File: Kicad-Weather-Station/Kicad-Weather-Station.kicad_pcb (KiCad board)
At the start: 2 copper layers, 100 x 50 mm, 64 parts, among them CON1 Solar Panel, J1 MicroSD, P1 CONN_01X25, P12 CONN_01X01, P2 CONN_01X25, P3 Rain Gauge, P4 Temperature/Humidity, P5 Wind Speed, P6 Air Pressure, P7 Battery, Q1 MMBT3904, Q2 MMBT3904, Q3 MMBT3906, Q4 SUD45P03-12-GE3, Q5 MMBT3904, Q6 MMBT3904, Q7 MMBT3904, Q8 MMBT3906, Q9 SUD45P03-12-GE3, U1 LMV324, U2 78M05, U3 TPS77033

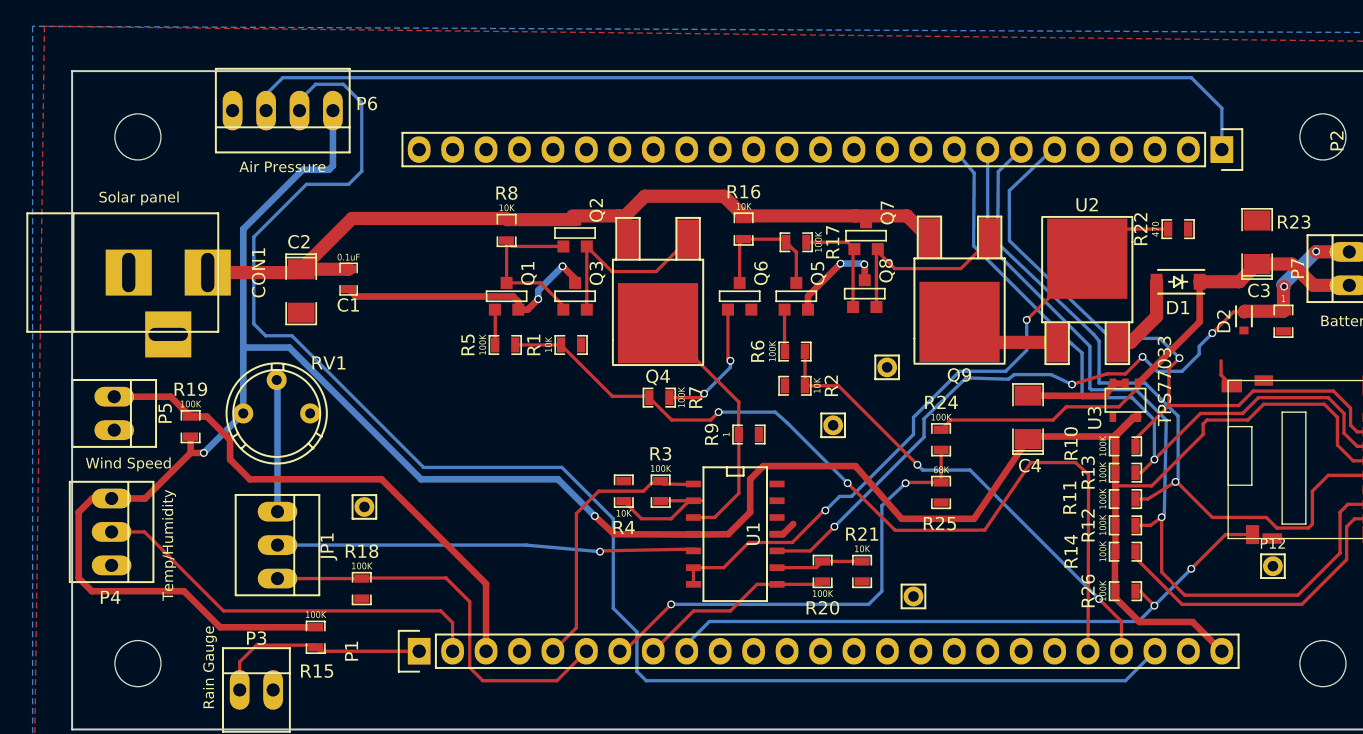
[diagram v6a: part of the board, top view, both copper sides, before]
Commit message: Update schematic and PCB to allow some sensors to be powered off.
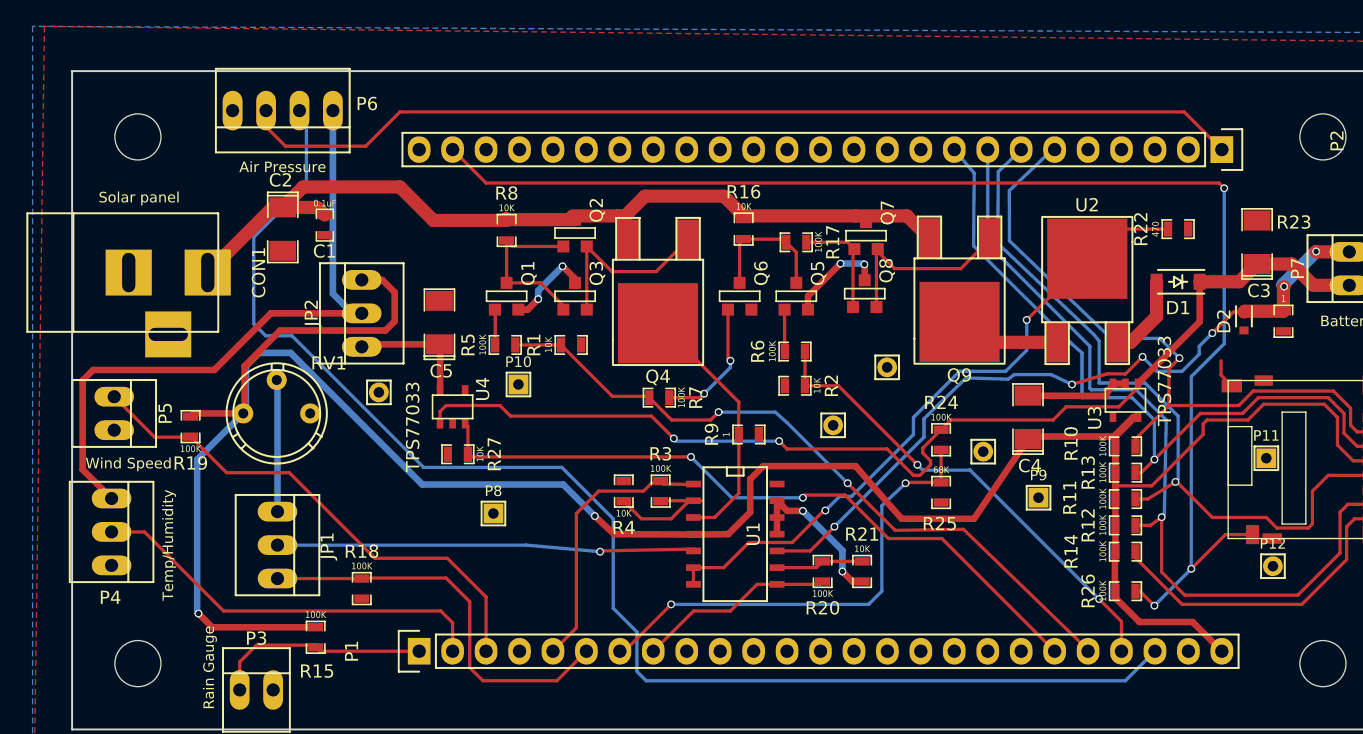
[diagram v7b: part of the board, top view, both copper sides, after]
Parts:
- added C5: 10uF, WeatherStation:SM1206POL, F.Cu at (87.9, 74.1)
- added JP2: JUMPER3, WeatherStation:PINHEAD1-3, F.Cu at (82.0, 73.4)
- added P10: CONN_01X01, WeatherStation:SIL-1, F.Cu at (93.9, 78.8)
- added P11: CONN_01X01, WeatherStation:SIL-1, F.Cu at (150.7, 84.4)
- added P8: CONN_01X01, WeatherStation:SIL-1, F.Cu at (92.0, 88.6)
- added P9: CONN_01X01, WeatherStation:SIL-1, F.Cu at (133.4, 87.4)
- added R27: 10K, WeatherStation:SM0603_Resistor, F.Cu at (89.3, 84.1)
- added U4: TPS77033, WeatherStation:SOT23-5, F.Cu at (88.9, 80.5)
- moved ? 12.2 mm to (129.2, 83.9)
- moved ? 8.77 mm to (83.3, 79.4)
- moved C2 4.90 mm to (76.0, 67.0)
- moved C1 4.48 mm to (79.2, 66.7)
- turned R19 to 90 degrees
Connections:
- net Net-(C3-Pad1) renamed Power
- C4 pad 1: +3.3V -> +3.3V-M
- J1 pad 11: PA8 -> PD2
- J1 pad 4: +3.3V -> +3.3V-M
- P1 pad 20: Net-(P1-Pad20) -> PB3
- P1 pad 25: +3.3V -> +3.3V-M
- P1 pad 9: PA8 -> Net-(P1-Pad9)
- P2 pad 24: Net-(P2-Pad24) -> PD2
- R10 pad 1: +3.3V -> +3.3V-M
- R11 pad 1: +3.3V -> +3.3V-M
- R12 pad 1: +3.3V -> +3.3V-M
- R13 pad 1: +3.3V -> +3.3V-M
- R14 pad 1: +3.3V -> +3.3V-M
- R15 pad 1: +3.3V -> +3.3V-M
- R19 pad 2: +3.3V -> +3.3V-M
- R26 pad 1: +3.3V -> +3.3V-M
- R26 pad 2: PA8 -> PD2
- RV1 pad 1: +3.3V -> +3.3V-M
- U1 pad 12: (no net) -> Earth
- U1 pad 13: (no net) -> Earth
- U1 pad 14: (no net) -> Net-(U1-Pad14)
- U1 pad 4: +3.3V -> +3.3V-M
- U3 pad 5: +3.3V -> +3.3V-M
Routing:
- net +3.3V-M: track 0.00 -> 190.7 mm, vias 0 -> 2
- net +3.3V: track 203.7 -> 49.9 mm, vias 2 -> 0
- net PD2: track 0.00 -> 101.3 mm, vias 0 -> 3
- net PB3: track 0.00 -> 53.3 mm, vias 0 -> 2
- net PA8: track 48.8 -> 0.00 mm, vias 2 -> 0
- net Power: track 38.9 -> 83.2 mm, vias 0 -> 2
- net PB4: track 66.3 -> 53.6 mm
- net PB6: track 115.0 -> 105.2 mm
- net Net-(C5-Pad1): track 0.00 -> 9.48 mm
- net Earth: track 40.3 -> 37.0 mm, vias 4 -> 6
- net PA2: track 40.1 -> 38.7 mm
- net Net-(C1-Pad1): track 68.7 -> 67.3 mm
- net Net-(P1-Pad9): track 0.00 -> 0.54 mm
- net PB7: track 78.4 -> 77.9 mm

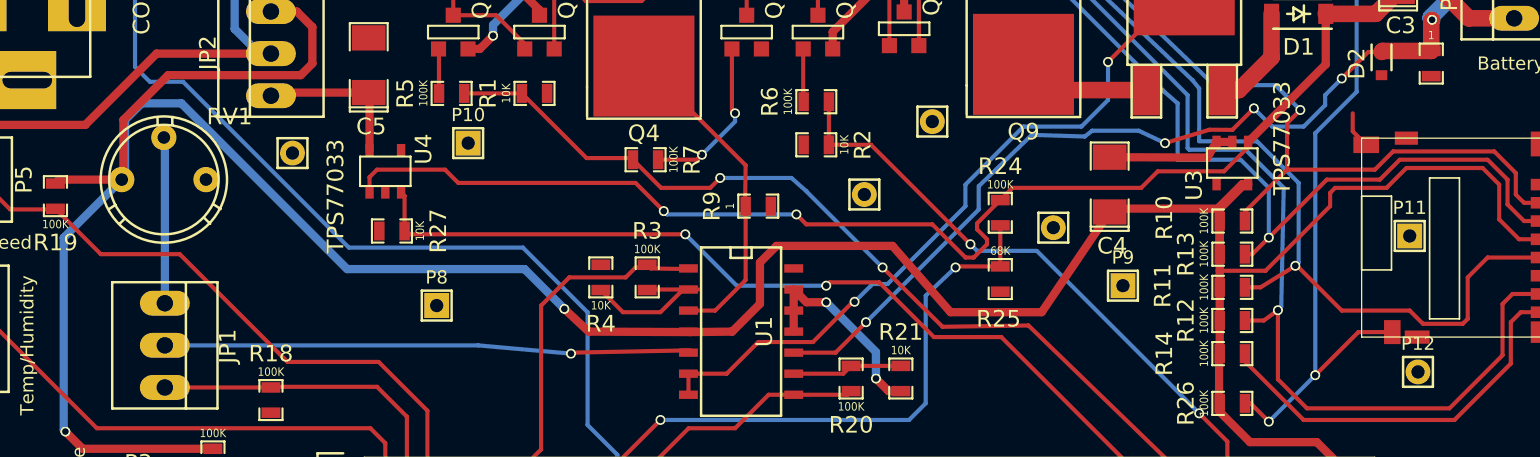
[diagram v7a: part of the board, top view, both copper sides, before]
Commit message: Clean up PCB footprints and generate gerbers.
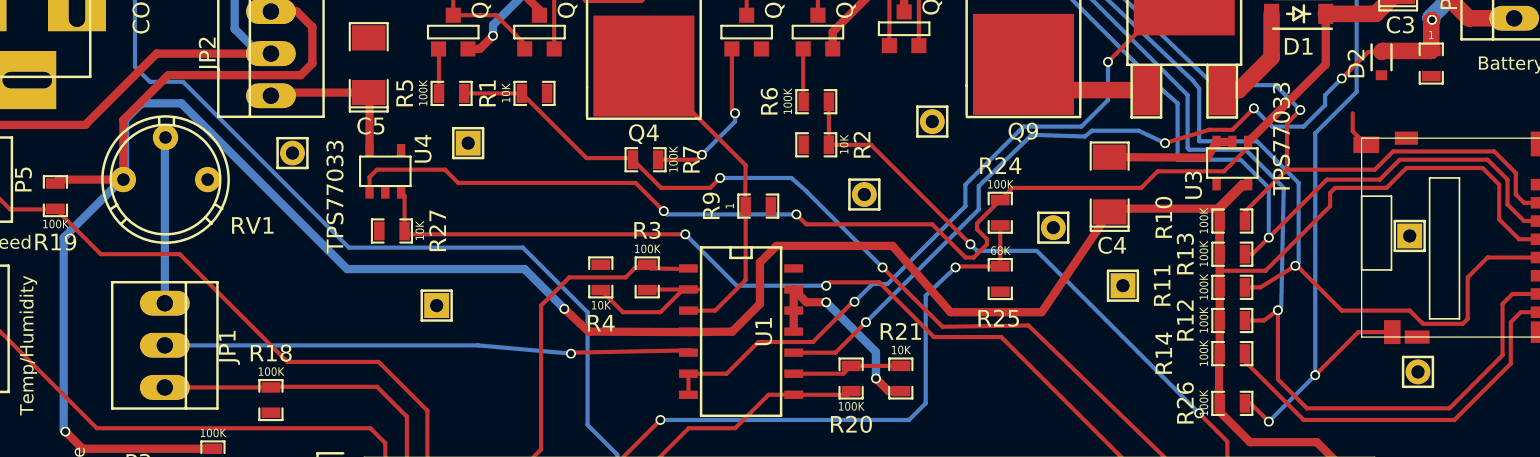
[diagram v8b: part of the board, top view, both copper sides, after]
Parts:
- RV1: footprint Potentiometers:Potentiometer_Bourns_3339P_Angular_ScrewUp -> WeatherStation:Potentiometer_Bourns_3339P_Angular_ScrewUp
- moved RV1 0.10 mm to (73.1, 81.0)
- renumbered P8 to ?, P9 to ?, P10 to ?, P11 to ?, P12 to ?
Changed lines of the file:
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@@
   (layers
     (0 F.Cu signal)
-    (31 B.Cu signal)
+    (31 B.Cu signal hide)
     (32 B.Adhes user hide)
     (33 F.Adhes user hide)
     (34 B.Paste user hide)
     (35 F.Paste user hide)
-    (36 B.SilkS user hide)
+    (36 B.SilkS user)
     (37 F.SilkS user)
-    (38 B.Mask user hide)
-    (39 F.Mask user hide)
-    (40 Dwgs.User user)
+    (38 B.Mask user)
+    (39 F.Mask user)
+    (40 Dwgs.User user hide)
     (41 Cmts.User user)
     (42 Eco1.User user hide)
@@
   )
   (setup
-    (last_trace_width 0.5)
+    (last_trace_width 0.25)
     (user_trace_width 0.5)
     (user_trace_width 1)
@@
     (visible_elements FFFFFF7F)
     (pcbplotparams
-      (layerselection 0x010f0_80000001)
-      (usegerberextensions false)
+      (layerselection 0x010fc_80000001)
+      (usegerberextensions true)
       (excludeedgelayer true)
       (linewidth 0.100000)
@@
       (effects (font (size 1 1) (thickness 0.15)))
     )
-    (fp_text value "Solar Panel" (at 0 -5.99948) (layer F.Fab)
+    (fp_text value "Solar Panel" (at 3.5 -4.3) (layer F.Fab)
       (effects (font (size 1 1) (thickness 0.15)))
     )
@@
       (effects (font (size 1 1) (thickness 0.15)))
     )
-    (fp_text value 1N4148 (at 0 1.7 90) (layer F.Fab)
+    (fp_text value 1N4148 (at -2.5 1.2 180) (layer F.Fab)
       (effects (font (size 1 1) (thickness 0.15)))
     )
@@
       (effects (font (size 1 1) (thickness 0.15)))
     )
-    (fp_text value CONN_01X25 (at 0 -3.1 90) (layer F.Fab)
+    (fp_text value CONN_01X25 (at -3.34 22.74 180) (layer F.Fab)
       (effects (font (size 1 1) (thickness 0.15)))
     )
@@
       (effects (font (size 1 1) (thickness 0.15)))
     )
-    (fp_text value CONN_01X25 (at 0 -3.1 270) (layer F.Fab)
+    (fp_text value CONN_01X25 (at -2.86 35.82 360) (layer F.Fab)
       (effects (font (size 1 1) (thickness 0.15)))
     )
@@
       (effects (font (size 1 1) (thickness 0.15)))
     )
-    (fp_text value "Rain Gauge" (at 0 3.81) (layer F.Fab)
+    (fp_text value "Rain Gauge" (at 0 5.5) (layer F.Fab)
       (effects (font (size 1 1) (thickness 0.15)))
     )
@@
       (effects (font (size 1 1) (thickness 0.15)))
     )
-    (fp_text value "Wind Speed" (at 0 3.81 270) (layer F.Fab)
+    (fp_text value "Wind Speed" (at 0 5.6 270) (layer F.Fab)
       (effects (font (size 1 1) (thickness 0.15)))
     )
@@
       (effects (font (size 1 1) (thickness 0.15)))
     )
-    (fp_text value "Air Pressure" (at 0 3.81 180) (layer F.Fab)
+    (fp_text value "Air Pressure" (at -0.2 5.4 180) (layer F.Fab)
       (effects (font (size 1 1) (thickness 0.15)))
     )
@@
     )
   )
-  (module Potentiometers:Potentiometer_Bourns_3339P_Angular_ScrewUp (layer F.Cu)
-    (at 73 81)
-    (descr "5/16, Round, Trimming, Potentiometer, Bourns, 3339")
-    (tags "5/16, Round, Trimming, Potentiometer, Bourns, 3339")
-    (fp_text reference RV1 (at 6.5 -3.8) (layer F.SilkS)
-      (effects (font (size 1 1) (thickness 0.15)))
-    )
-    (fp_text value 100K (at 2.54 6.35) (layer F.Fab)
-      (effects (font (size 1 1) (thickness 0.15)))
-    )
-    (fp_line (start 5.334 2.667) (end 4.953 2.286) (layer F.SilkS) (width 0.15))
-    (fp_line (start 5.969 1.778) (end 5.588 1.524) (layer F.SilkS) (width 0.15))
-    (fp_line (start -0.762 1.778) (end -0.381 1.524) (layer F.SilkS) (width 0.15))
-    (fp_line (start -0.127 2.667) (end 0.127 2.413) (layer F.SilkS) (width 0.15))
-    (fp_line (start 3.048 -3.302) (end 3.048 -3.683) (layer F.SilkS) (width 0.15))
-    (fp_line (start 2.159 -3.302) (end 2.159 -3.683) (layer F.SilkS) (width 0.15))
-    (fp_circle (center 2.54 0) (end 5.842 0) (layer F.SilkS) (width 0.15))
-    (fp_circle (center 2.54 0) (end 6.35 0) (layer F.SilkS) (width 0.15))
-    (pad 2 thru_hole circle (at 2.54 -2.54) (size 1.524 1.524) (drill 0.762) (layers *.Cu *.Mask F.SilkS)
-      (net 6 "Net-(JP1-Pad1)"))
-    (pad 1 thru_hole circle (at 0 0) (size 1.524 1.524) (drill 0.762) (layers *.Cu *.Mask F.SilkS)
-      (net 70 +3.3V-M))
-    (pad 3 thru_hole circle (at 5.08 0) (size 1.524 1.524) (drill 0.762) (layers *.Cu *.Mask F.SilkS)
-      (net 2 Earth))
-    (model Potentiometers.3dshapes/Potentiometer_Bourns_3339P_Angular_ScrewUp.wrl
-      (at (xyz 0 0 0))
-      (scale (xyz 1 1 1))
-      (rotate (xyz 0 0 0))
-    )
-  )
   (module WeatherStation:MountingHole_3-5mm (layer F.Cu)
     (at 65 100)
@@
       (effects (font (size 1 1) (thickness 0.15)))
     )
-    (fp_text value MountingHole_3-5mm (at 0 5.00126) (layer F.Fab)
+    (fp_text value MountingHole_3-5mm (at -0.1 5.9) (layer F.Fab)
       (effects (font (size 1 1) (thickness 0.15)))
     )
@@
       (effects (font (size 1 1) (thickness 0.15)))
     )
-    (fp_text value MountingHole_3-5mm (at 0 5.00126) (layer F.Fab)
+    (fp_text value MountingHole_3-5mm (at 0.2 5.8) (layer F.Fab)
       (effects (font (size 1 1) (thickness 0.15)))
     )
@@
       (effects (font (size 1 1) (thickness 0.15)))
     )
-    (fp_text value MountingHole_3-5mm (at 0 5.00126) (layer F.Fab)
+    (fp_text value MountingHole_3-5mm (at -0.8 -6.1) (layer F.Fab)
       (effects (font (size 1 1) (thickness 0.15)))
     )
@@
       (effects (font (size 1 1) (thickness 0.15)))
     )
-    (fp_text value MountingHole_3-5mm (at 0 5.00126) (layer F.Fab)
+    (fp_text value MountingHole_3-5mm (at 0.1 -6.1) (layer F.Fab)
       (effects (font (size 1 1) (thickness 0.15)))
     )
@@
     (tags "CONN DEV")
     (zone_connect 2)
-    (fp_text reference P12 (at 0 -1.7) (layer F.SilkS)
+    (fp_text reference "" (at 0 -1.7) (layer F.SilkS)
       (effects (font (size 0.8 0.8) (thickness 0.15)))
     )
@@
     (tags "CONN DEV")
     (zone_connect 2)
-    (fp_text reference P8 (at 0 -1.7) (layer F.SilkS)
+    (fp_text reference "" (at 0 -1.7) (layer F.SilkS)
       (effects (font (size 0.8 0.8) (thickness 0.15)))
     )
@@
     (tags "CONN DEV")
     (zone_connect 2)
-    (fp_text reference P9 (at 0 -1.7) (layer F.SilkS)
+    (fp_text reference "" (at 0 -1.7) (layer F.SilkS)
       (effects (font (size 0.8 0.8) (thickness 0.15)))
     )
@@
     (tags "CONN DEV")
     (zone_connect 2)
-    (fp_text reference P10 (at 0 -1.7) (layer F.SilkS)
+    (fp_text reference "" (at 1.3 2.5) (layer F.SilkS)
       (effects (font (size 0.8 0.8) (thickness 0.15)))
     )
@@
     (tags "CONN DEV")
     (zone_connect 2)
-    (fp_text reference P11 (at 0 -1.7) (layer F.SilkS)
+    (fp_text reference "" (at 0 -1.7) (layer F.SilkS)
       (effects (font (size 0.8 0.8) (thickness 0.15)))
     )
@@
       (rotate (xyz 0 0 0))
     )
+  )
+  (module WeatherStation:Potentiometer_Bourns_3339P_Angular_ScrewUp (layer F.Cu)
+    (at 73.1 81)
+    (descr "5/16, Round, Trimming, Potentiometer, Bourns, 3339")
+    (tags "5/16, Round, Trimming, Potentiometer, Bourns, 3339")
+    (fp_text reference RV1 (at 7.8 2.8) (layer F.SilkS)
+      (effects (font (size 1 1) (thickness 0.15)))
+    )
+    (fp_text value 100K (at 2.54 6.35) (layer F.Fab)
+      (effects (font (size 1 1) (thickness 0.15)))
+    )
+    (fp_line (start 5.334 2.667) (end 4.953 2.286) (layer F.SilkS) (width 0.15))
+    (fp_line (start 5.969 1.778) (end 5.588 1.524) (layer F.SilkS) (width 0.15))
+    (fp_line (start -0.762 1.778) (end -0.381 1.524) (layer F.SilkS) (width 0.15))
+    (fp_line (start -0.127 2.667) (end 0.127 2.413) (layer F.SilkS) (width 0.15))
+    (fp_line (start 3.048 -3.302) (end 3.048 -3.683) (layer F.SilkS) (width 0.15))
+    (fp_line (start 2.159 -3.302) (end 2.159 -3.683) (layer F.SilkS) (width 0.15))
+    (fp_circle (center 2.54 0) (end 5.842 0) (layer F.SilkS) (width 0.15))
+    (fp_circle (center 2.54 0) (end 6.35 0) (layer F.SilkS) (width 0.15))
+    (pad 2 thru_hole circle (at 2.54 -2.54) (size 1.524 1.524) (drill 0.762) (layers *.Cu *.Mask F.SilkS)
+      (net 6 "Net-(JP1-Pad1)"))
+    (pad 1 thru_hole circle (at 0 0) (size 1.524 1.524) (drill 0.762) (layers *.Cu *.Mask F.SilkS)
+      (net 70 +3.3V-M))
+    (pad 3 thru_hole circle (at 5.08 0) (size 1.524 1.524) (drill 0.762) (layers *.Cu *.Mask F.SilkS)
+      (net 2 Earth))
+    (model Potentiometers.3dshapes/Potentiometer_Bourns_3339P_Angular_ScrewUp.wrl
+      (at (xyz 0 0 0))
+      (scale (xyz 1 1 1))
+      (rotate (xyz 0 0 0))
+    )
